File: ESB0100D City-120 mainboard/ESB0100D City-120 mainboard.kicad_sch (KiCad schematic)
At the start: 19 parts, among them J100 Conn_01x01, J101 Conn_01x01, J103 Front wheel dropoff, J104 Odometers, J105 Siren, J106 Terminal board, J170 Charger port, J400 Wire sensors, J501 Bumpers, J505 9V battery, J704 Drive motors, J802 Mow motors

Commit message: Daily save
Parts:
- added R20: 1K, symbol Device:R_Pack04
- added U5: 74LS259, symbol 74xx:74LS259
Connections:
- new net: R20.8 (R1.2), U5.4 (Q0)
- new net: R20.7 (R2.2), U5.5 (Q1)
- new net: R20.6 (R3.2), U5.6 (Q2)
- new net: R20.5 (R4.2), U5.7 (Q3)
- new net MOW_153_MUX_1_A: R20.1 (R1.1)
- new net MOW_153_MUX_2_A: R20.2 (R2.1)
- new net MOW_153_MUX_3_A: R20.3 (R3.1)
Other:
- sheet Mow motor driver renamed Mow motor driver left
- added sheet Drive motors (drive_motors.kicad_sch)
- added sheet H8S MCU (H8S MCU.kicad_sch)
- added sheet Mow motor driver mid (mow_motor_driver.kicad_sch)
- added sheet Mow motor driver right (mow_motor_driver.kicad_sch)

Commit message: Repo update
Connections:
- net RX0: now reaches J106.2 (Pin_2)
- net TX0: now reaches J106.3 (Pin_3)
- net RX1: now reaches J106.4 (Pin_4)
- net TX1: now reaches J106.5 (Pin_5)
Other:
- added sheet Connector board ESB0021E (ESB0021E.kicad_sch)
- moved on the sheet: J106

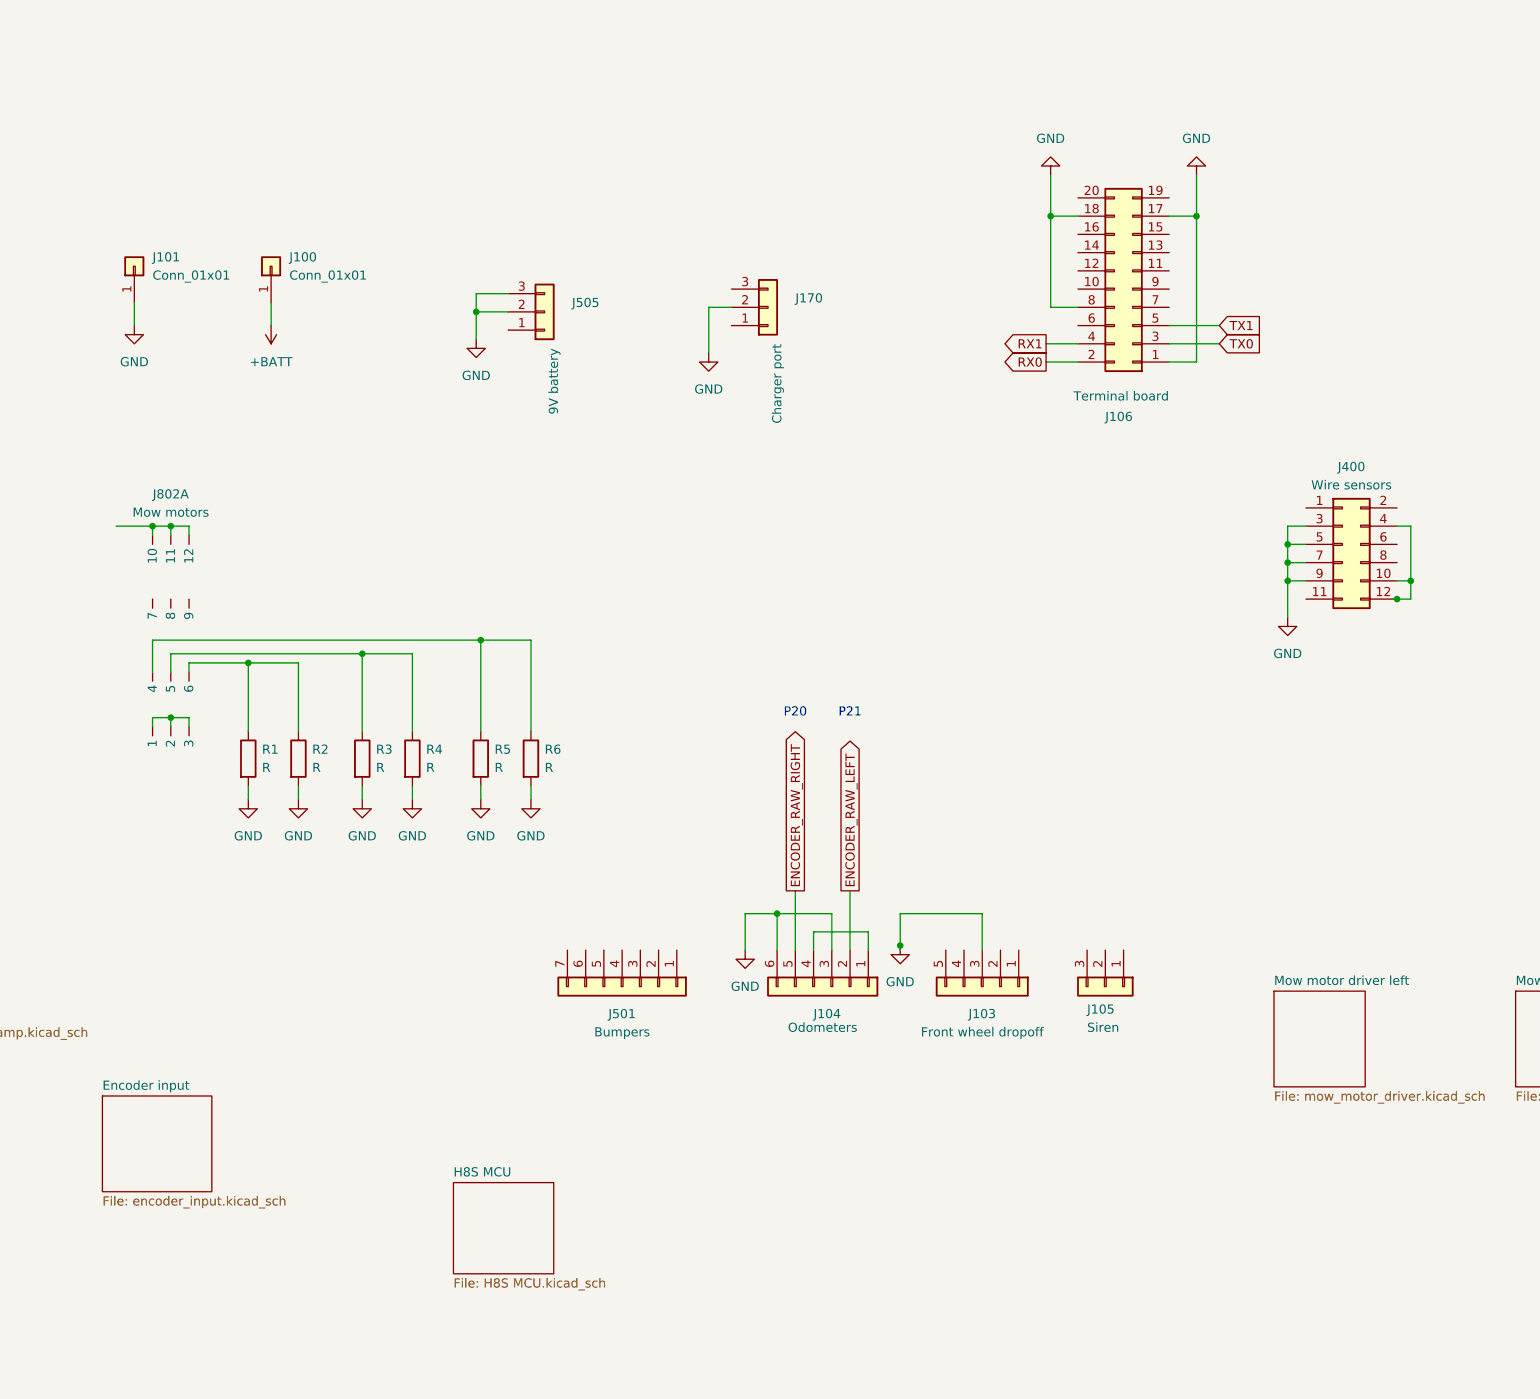
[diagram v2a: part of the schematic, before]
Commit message: Add bumper an slippage sensor connections
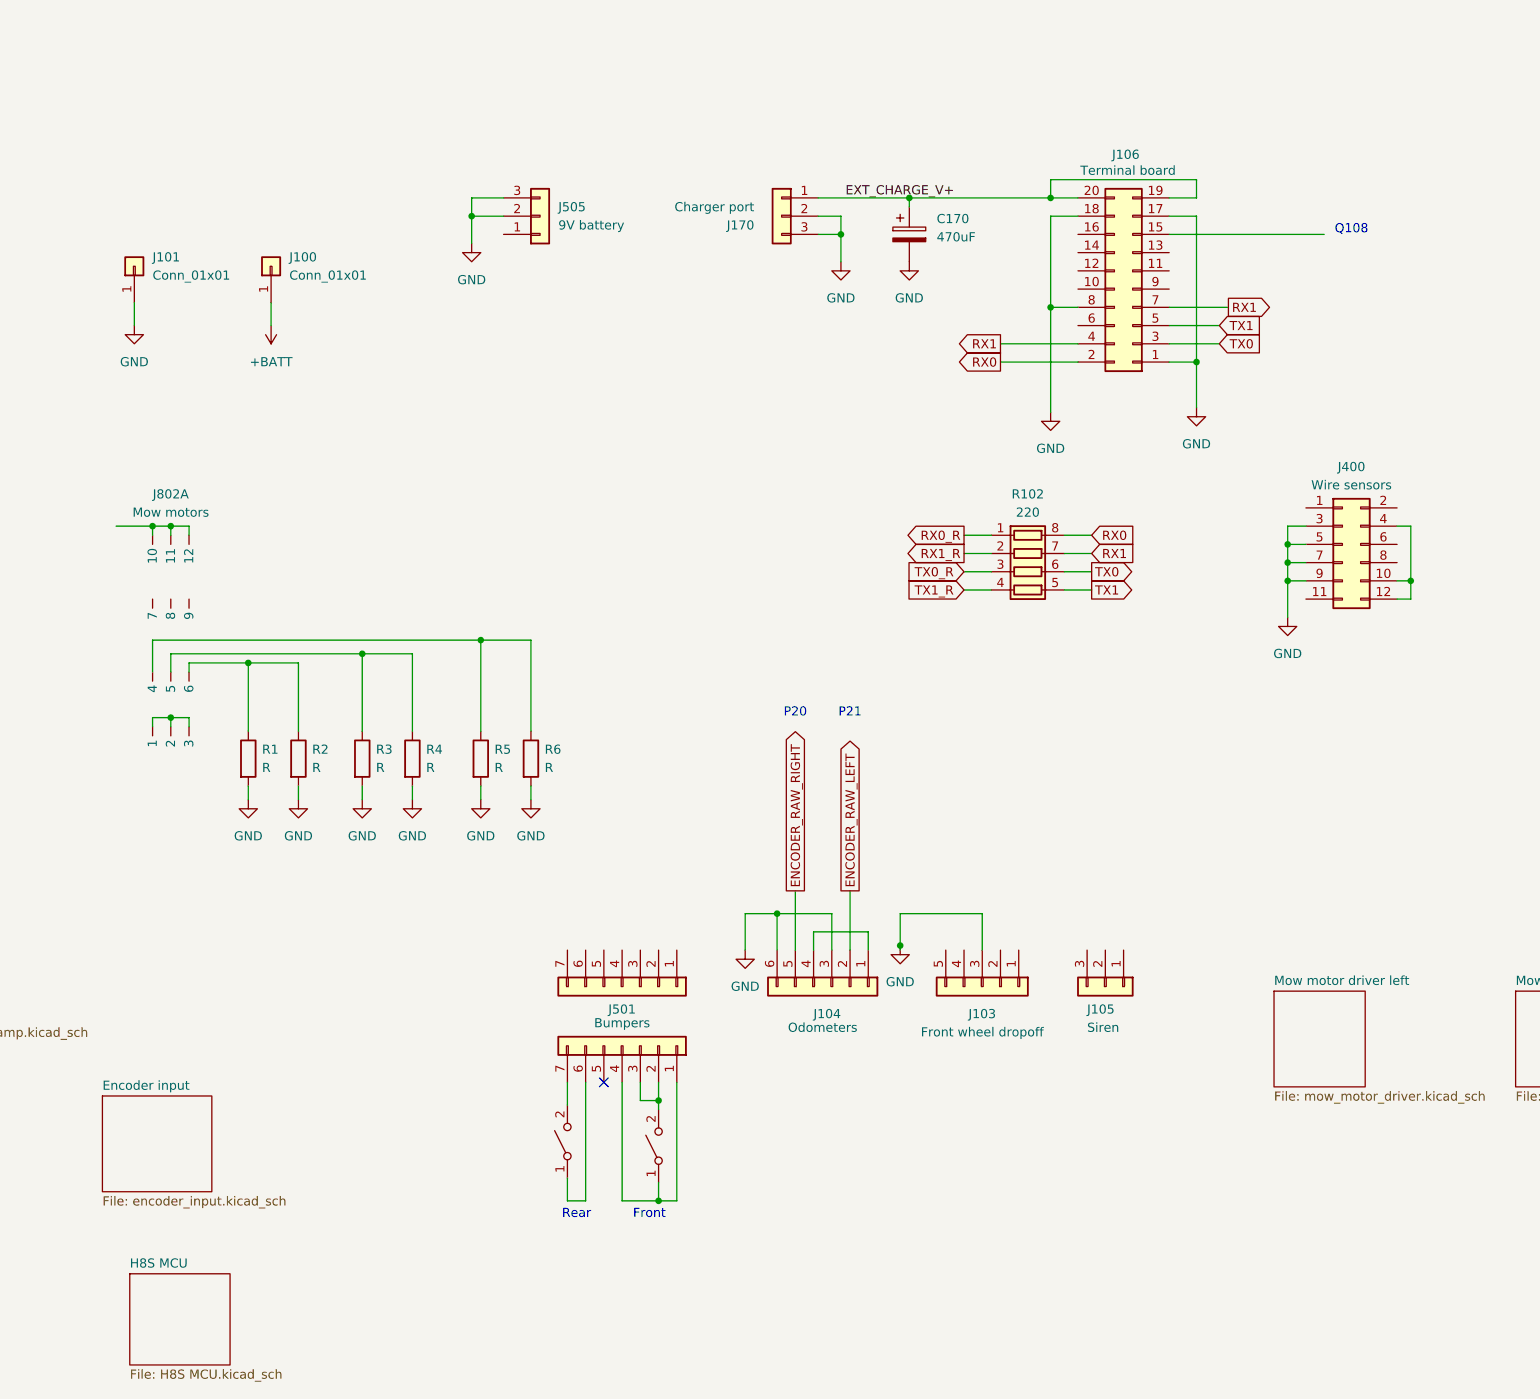
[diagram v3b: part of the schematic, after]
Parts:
- added C170: 470uF, symbol Device:C_Polarized
- added J7: Conn_01x07, symbol Connector_Generic:Conn_01x07
- added R102: 220, symbol Device:R_Pack04
- added SW1, SW2: SW_SPST, symbol Switch:SW_SPST
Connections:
- net GND: now also J170.3 (Pin_3), C170.2
- net RX0: now also R102.8 (R1.2)
- net RX1: now also J106.7 (Pin_7), R102.7 (R2.2)
- net TX0: now also R102.6 (R3.2)
- net TX1: now also R102.5 (R4.2)
- net EXT_CHARGE_V+: now reaches J106.19 (Pin_19)
- net EXT_CHARGE_V+: now also J106.20 (Pin_20), J170.1 (Pin_1), C170.1
- new net: J7.1 (Pin_1), J7.4 (Pin_4), SW1.1 (A)
- new net: J7.2 (Pin_2), J7.3 (Pin_3), SW1.2 (B)
- new net: J7.6 (Pin_6), SW2.1 (A)
- new net: J7.7 (Pin_7), SW2.2 (B)
- new net RX0_R: R102.1 (R1.1)
- new net RX1_R: R102.2 (R2.1)
- new net TX0_R: R102.3 (R3.1)
- new net TX1_R: R102.4 (R4.1)
- no-connect marks 0 -> 1
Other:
- note added: "Front"
- note added: "Q108"
- note added: "Rear"
- moved on the sheet: J170, J505
